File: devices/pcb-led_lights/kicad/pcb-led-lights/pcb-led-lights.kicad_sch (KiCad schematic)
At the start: 29 parts, among them J1 Screw_Terminal_01x12, Q1 SUD40N06-25L, Q2 SUD40N06-25L, Q3 SUD40N06-25L, Q4 SUD40N06-25L, Q5 SUD40N06-25L, Q6 SUD40N06-25L, Q7 SUD40N06-25L, U1 AP63203WU, U2 ESP32-WROOM-32

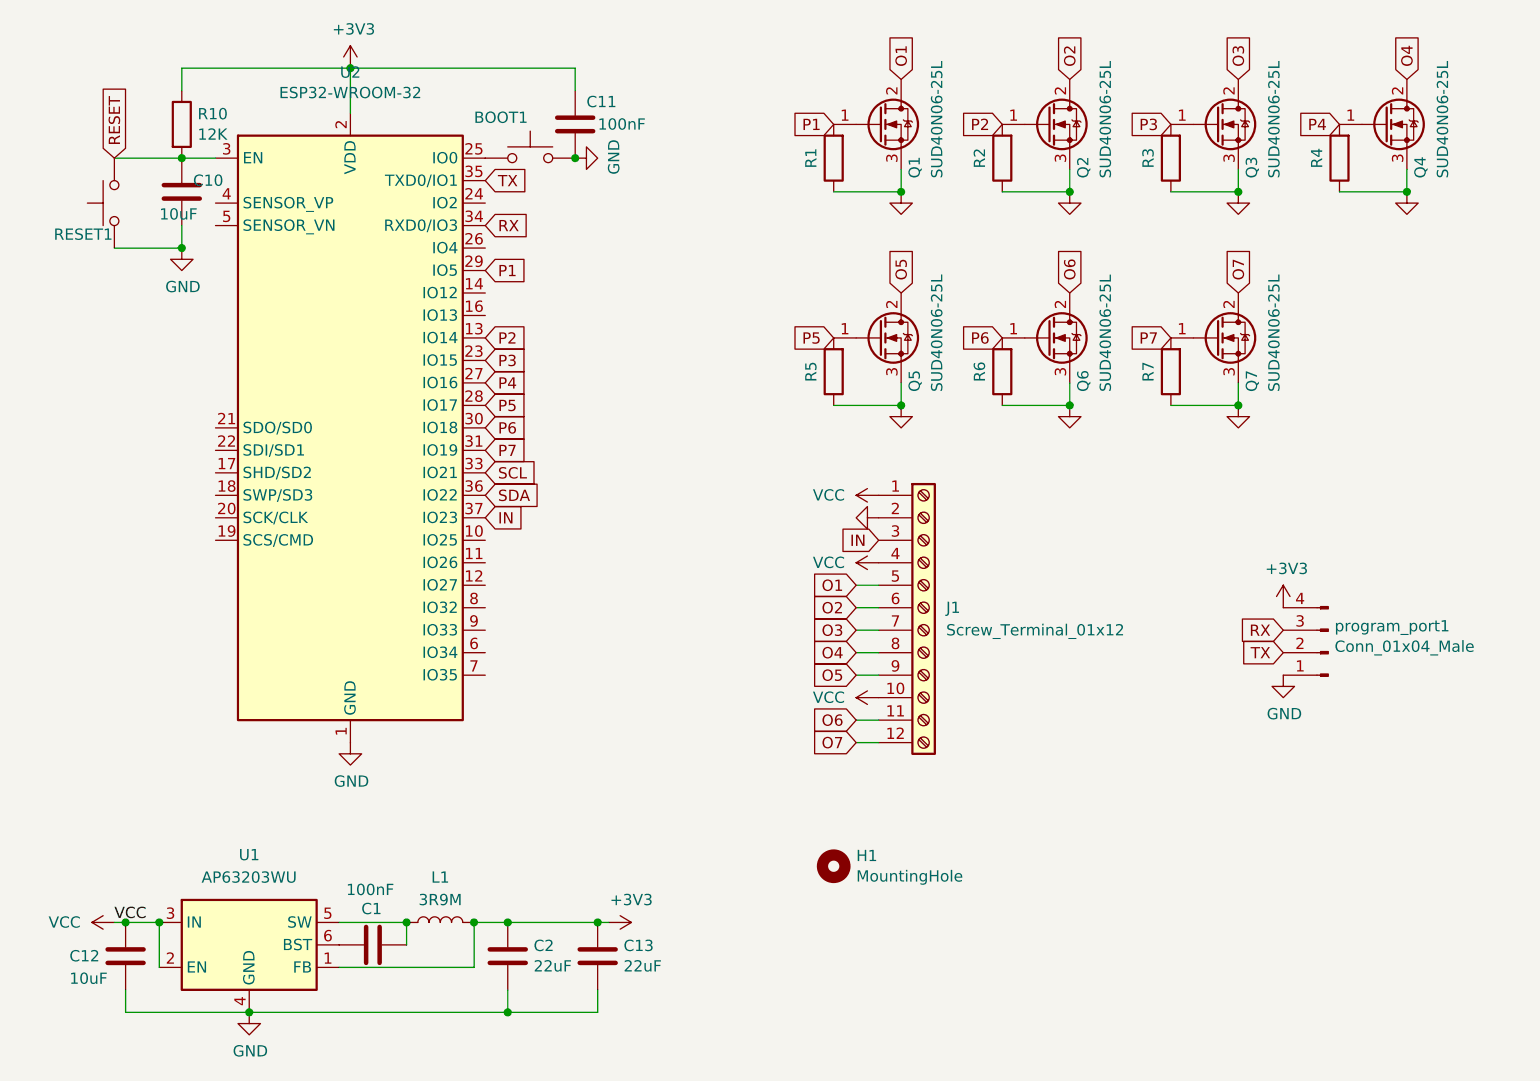
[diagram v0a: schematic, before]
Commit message: use esp32-c6
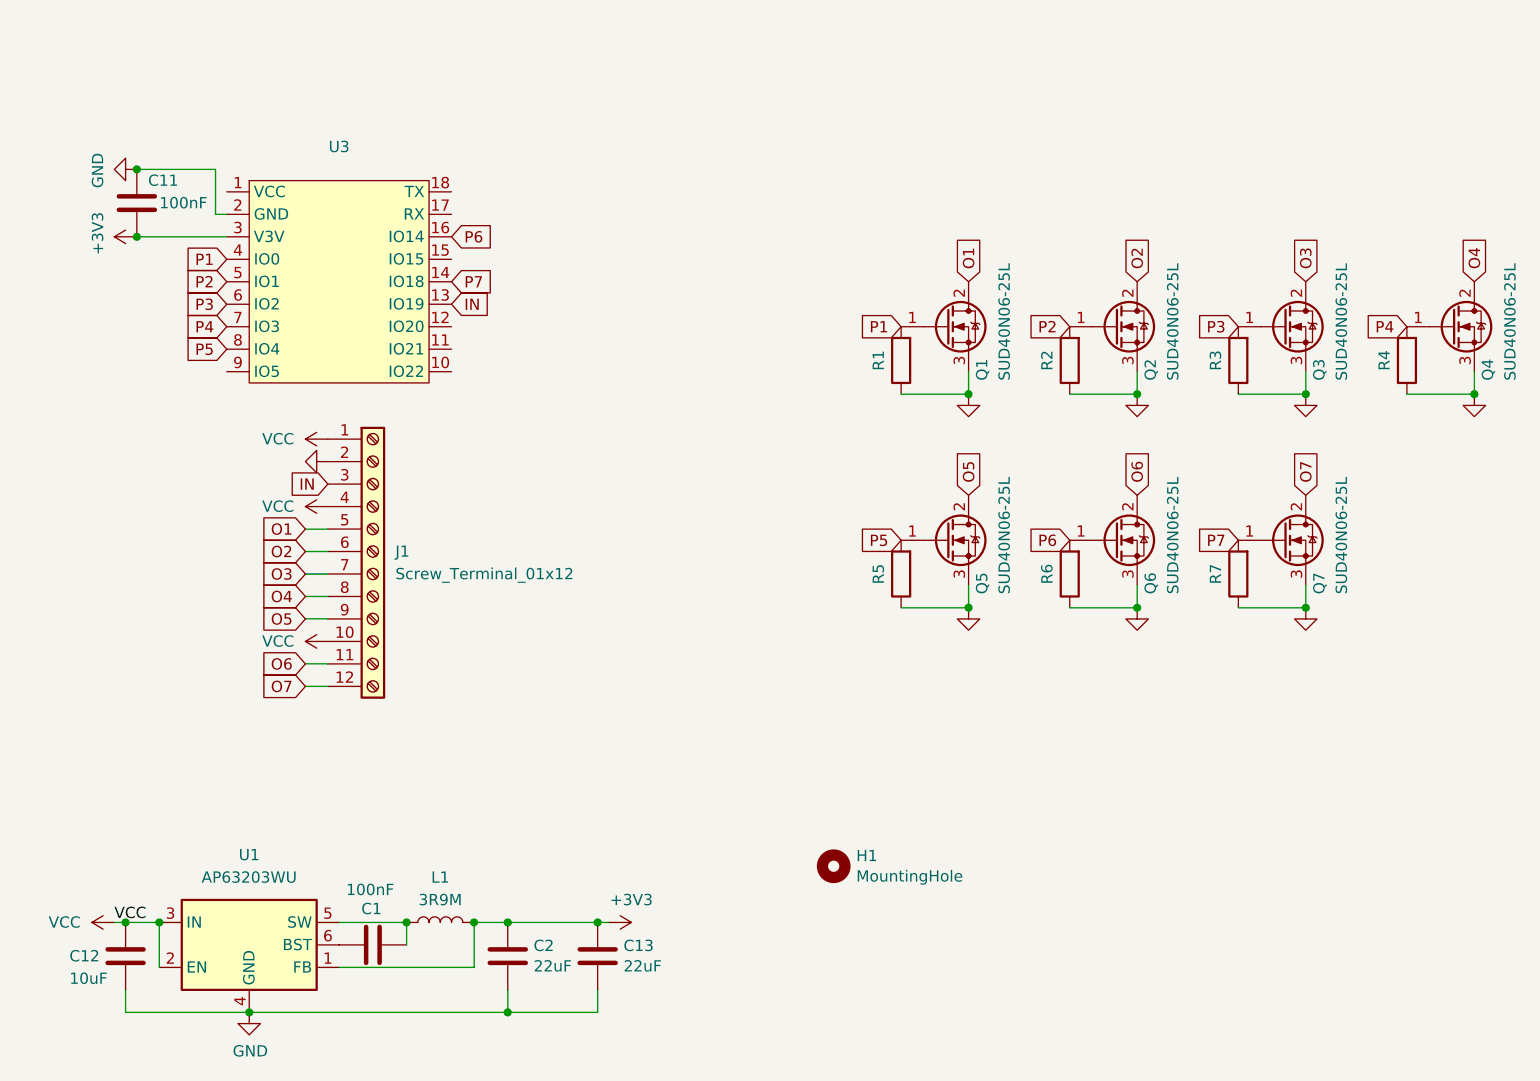
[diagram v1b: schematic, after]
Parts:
- removed BOOT1, RESET1: SW_Push, Button_Switch_SMD:SW_SPST_PTS810, symbol Switch:SW_Push
- removed C10: 10uF, Capacitor_SMD:C_0805_2012Metric, symbol Device:C
- removed R10: 12K, Resistor_SMD:R_0805_2012Metric, symbol Device:R
- removed U2: ESP32-WROOM-32, RF_Module:ESP32-WROOM-32, symbol RF_Module:ESP32-WROOM-32
- removed program_port1: Conn_01x04_Male, Connector_PinHeader_2.54mm:PinHeader_1x04_P2.54mm_Vertical, symbol Connector:Conn_01x04_Male
- added U3: ~, Waveshare-ESP32:Waveshare-ESP32-C6-Zero, symbol Waveshare-ESP32:Waveshare-ESP32-C6-Zero
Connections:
- net +3V3: now also C11.1, U3.3 (V3V); no longer C11.2
- net GND: now also C11.2, U3.2 (GND); no longer C11.1
- net IN: now also U3.13 (IO19)
- net P1: now also U3.4 (IO0)
- net P2: now also U3.5 (IO1)
- net P3: now also U3.6 (IO2)
- net P4: now also U3.7 (IO3)
- net P5: now also U3.8 (IO4)
- net P6: now also U3.16 (IO14)
- net P7: now also U3.14 (IO18)
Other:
- moved on the sheet: C11, J1, Q1, Q2, Q3, Q4, Q5, Q6, Q7, R1, R2, R3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

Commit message: add diode
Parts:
- added D1: US2MA, Diode_SMD:D_SMA, symbol Diode:US2MA
- R1, R2, R3, R4, R5, R6, R7: value R -> 12K
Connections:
- net VCC: now also D1.2 (A); no longer C12.2, U1.2 (EN), U1.3 (IN)
- new net: C12.2, D1.1 (K), U1.2 (EN), U1.3 (IN)
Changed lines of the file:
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@@
 		(title "LED Lights")
 		(date "2025-08-19")
-		(rev "9")
+		(rev "10")
 	)
 	(junction
@@
 	(wire
 		(pts
-			(xy 22.86 116.84) (xy 24.13 116.84)
-		)
-		(stroke
-			(width 0)
-			(type default)
-		)
-	)
-	(wire
-		(pts
 			(xy 44.45 87.63) (xy 46.99 87.63)
 		)
@@
 	)
 	(label "VCC"
-		(at 22.86 116.84 0)
+		(at 12.7 119.38 0)
 		(effects
 			(font
@@
 	(symbol
 		(lib_id "power:VCC")
-		(at 22.86 116.84 90)
+		(at 16.51 116.84 90)
 		(unit 1)
 		(exclude_from_sim no)
@@
 		(on_board yes)
 		(dnp no)
-		(fields_autoplaced yes)
 		(property "Reference" "#PWR02"
-			(at 26.67 116.84 0)
+			(at 20.32 116.84 0)
 			(effects
 				(font
@@
 		)
 		(property "Value" "VCC"
-			(at 19.05 116.8399 90)
+			(at 16.51 115.062 90)
 			(effects
 				(font
@@
 		)
 		(property "Footprint" ""
-			(at 22.86 116.84 0)
+			(at 16.51 116.84 0)
 			(effects
 				(font
@@
 		)
 		(property "Datasheet" ""
-			(at 22.86 116.84 0)
+			(at 16.51 116.84 0)
 			(effects
 				(font
@@
 		)
 		(property "Description" "Power symbol creates a global label with name \"VCC\""
-			(at 22.86 116.84 0)
+			(at 16.51 116.84 0)
 			(effects
 				(font
@@
 			)
 		)
-		(property "Value" "R"
+		(property "Value" "12K"
 			(at 128.6026 53.34 90)
 			(effects
@@
 			)
 		)
-		(property "Value" "R"
+		(property "Value" "12K"
 			(at 109.5526 77.47 90)
 			(effects
@@
 			)
 		)
-		(property "Value" "R"
+		(property "Value" "12K"
 			(at 128.6026 77.47 90)
 			(effects
@@
 	)
 	(symbol
+		(lib_id "Diode:US2MA")
+		(at 20.32 116.84 180)
+		(unit 1)
+		(exclude_from_sim no)
+		(in_bom yes)
+		(on_board yes)
+		(dnp no)
+		(fields_autoplaced yes)
+		(property "Reference" "D1"
+			(at 20.32 110.49 0)
+			(effects
+				(font
+					(size 1.27 1.27)
+				)
+			)
+		)
+		(property "Value" "US2MA"
+			(at 20.32 113.03 0)
+			(effects
+				(font
+					(size 1.27 1.27)
+				)
+			)
+		)
+		(property "Footprint" "Diode_SMD:D_SMA"
+			(at 20.32 112.395 0)
+			(effects
+				(font
+					(size 1.27 1.27)
+				)
+				(hide yes)
+			)
+		)
+		(property "Datasheet" "https://www.onsemi.com/pub/Collateral/US2AA-D.PDF"
+			(at 20.32 116.84 0)
+			(effects
+				(font
+					(size 1.27 1.27)
+				)
+				(hide yes)
+			)
+		)
+		(property "Description" "1000V, 1.5A, General Purpose Rectifier Diode, SMA(DO-214AC)"
+			(at 20.32 116.84 0)
+			(effects
+				(font
+					(size 1.27 1.27)
+				)
+				(hide yes)
+			)
+		)
+		(property "Sim.Device" "D"
+			(at 20.32 116.84 0)
+			(effects
+				(font
+					(size 1.27 1.27)
+				)
+				(hide yes)
+			)
+		)
+		(property "Sim.Pins" "1=K 2=A"
+			(at 20.32 116.84 0)
+			(effects
+				(font
+					(size 1.27 1.27)
+				)
+				(hide yes)
+			)
+		)
+		(pin "1"
+		)
+		(pin "2"
+		)
+		(instances
+			(project ""
+				(path "/e63e39d7-6ac0-4ffd-8aa3-1841a4541b55"
+					(reference "D1")
+					(unit 1)
+				)
+			)
+		)
+	)
+	(symbol
 		(lib_id "power:GND")
 		(at 176.53 57.15 0)
@@
 			)
 		)
-		(property "Value" "R"
+		(property "Value" "12K"
 			(at 109.5526 53.34 90)
 			(effects
@@
 			)
 		)
-		(property "Value" "R"
+		(property "Value" "12K"
 			(at 147.6526 77.47 90)
 			(effects
@@
 			)
 		)
-		(property "Value" "R"
+		(property "Value" "12K"
 			(at 166.7026 53.34 90)
 			(effects
@@
 			)
 		)
-		(property "Value" "R"
+		(property "Value" "12K"
 			(at 147.6526 53.34 90)
 			(effects
